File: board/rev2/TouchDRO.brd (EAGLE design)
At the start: 50.8 x 50.8 mm, 24 parts, among them U2 VREG_33, U3 VREG_5

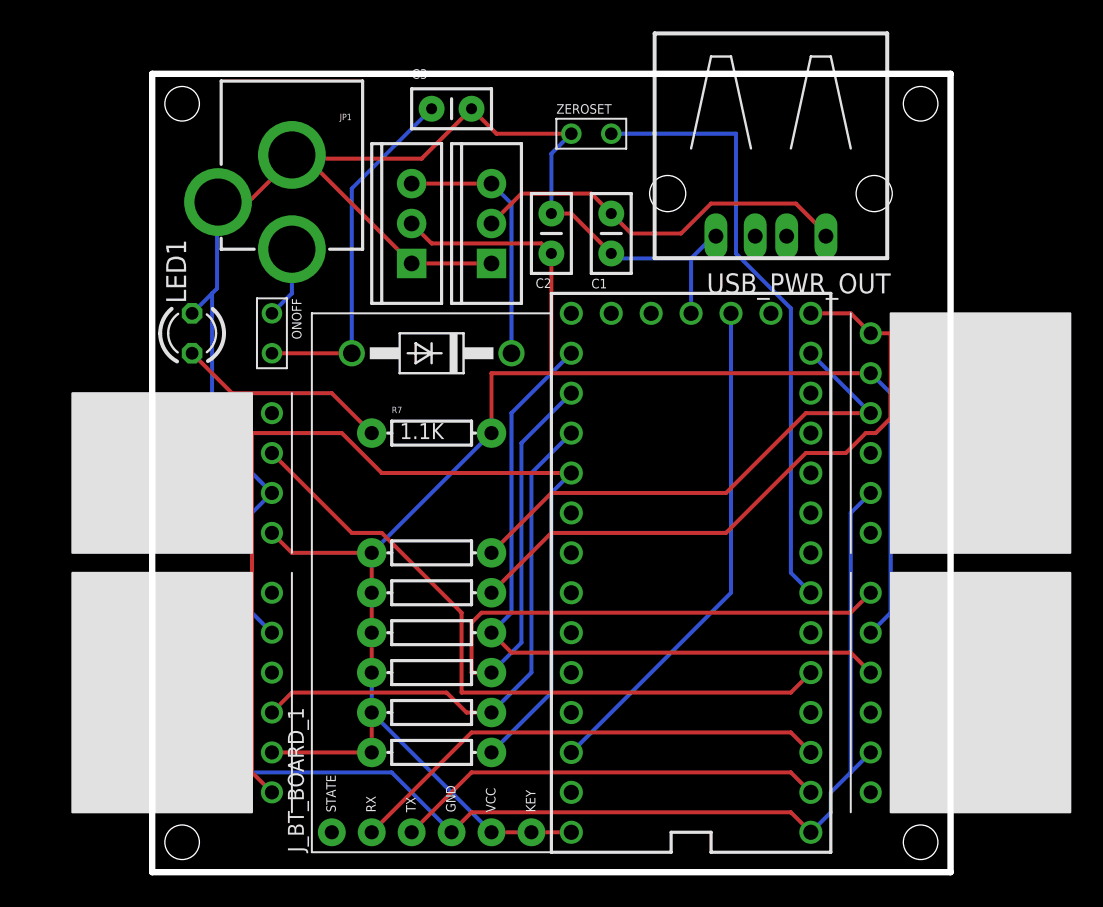
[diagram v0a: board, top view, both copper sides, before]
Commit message: adding additional caps to voltage regulator outputs
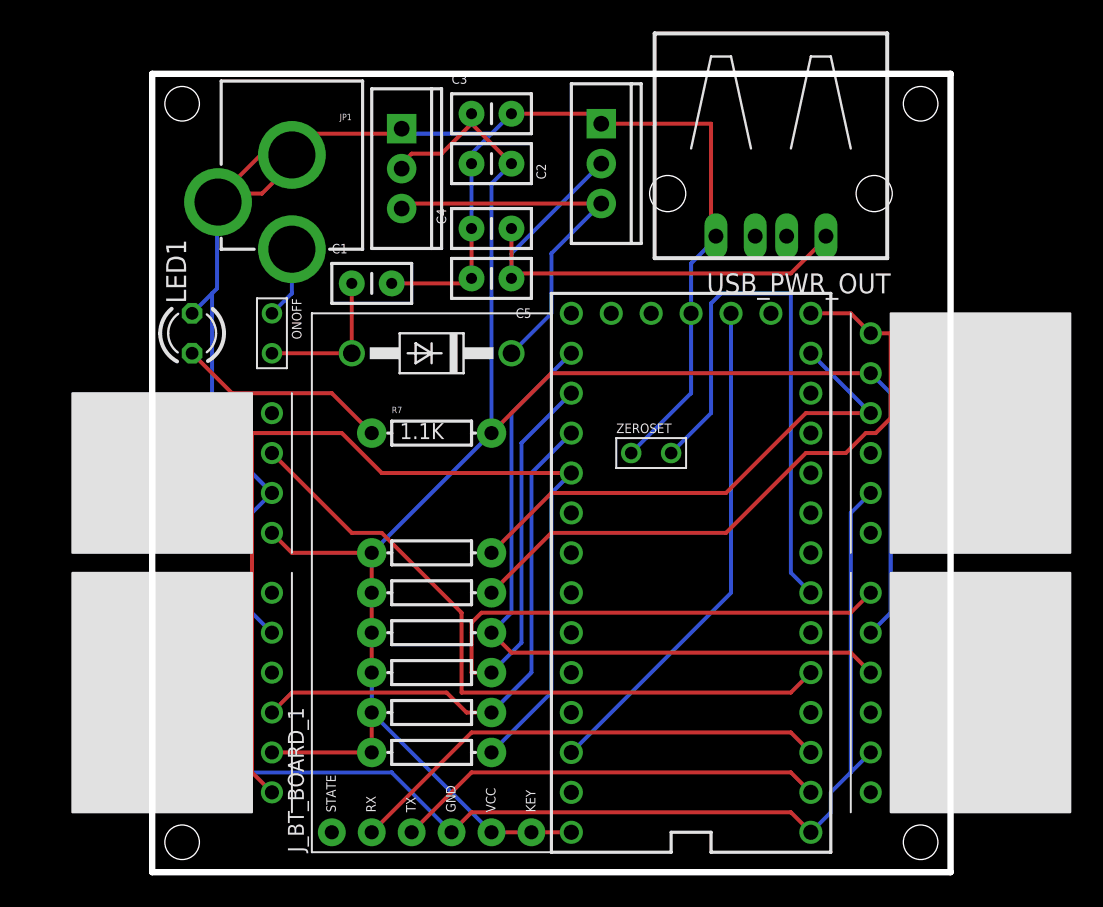
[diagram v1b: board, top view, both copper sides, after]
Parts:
- added C4: 10uF, SparkFun-Passives:CAP-PTH-SMALLEZ
- added C5: 0.1uF, SparkFun-Passives:CAP-PTH-SMALLEZ
- C1: value 10uF -> 100uF
- C3: value 100uF -> 0.1uF
- moved ZEROSET 20.7 mm to (33.0, 26.7)
- moved C1 17.1 mm to (12.7, 37.5), turned to 0 degrees
- moved U3 7.96 mm to (28.6, 45.1), turned to 270 degrees
- moved C2 6.25 mm to (22.9, 45.1), turned to 180 degrees
- moved U2 3.55 mm to (15.9, 44.8), turned to 270 degrees
- moved C3 2.56 mm to (20.3, 48.3)
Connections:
- net +3V3: now also C3.1
- net +5V: now also C4.1, C5.1; no longer C1.1
- net GND: now also C4.2, C5.2
- net ONOFF: now also C1.1; no longer C3.1
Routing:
- net GND: track 168.1 -> 184.3 mm
- net ONOFF: track 22.7 -> 9.52 mm
- net +5V: track 24.9 -> 33.9 mm
- net D1: track 16.4 -> 24.9 mm
- net +3V3: track 115.4 -> 123.5 mm
- net ZSET: track 39.1 -> 35.5 mm

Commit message: rerouting z-axis signals to new pins
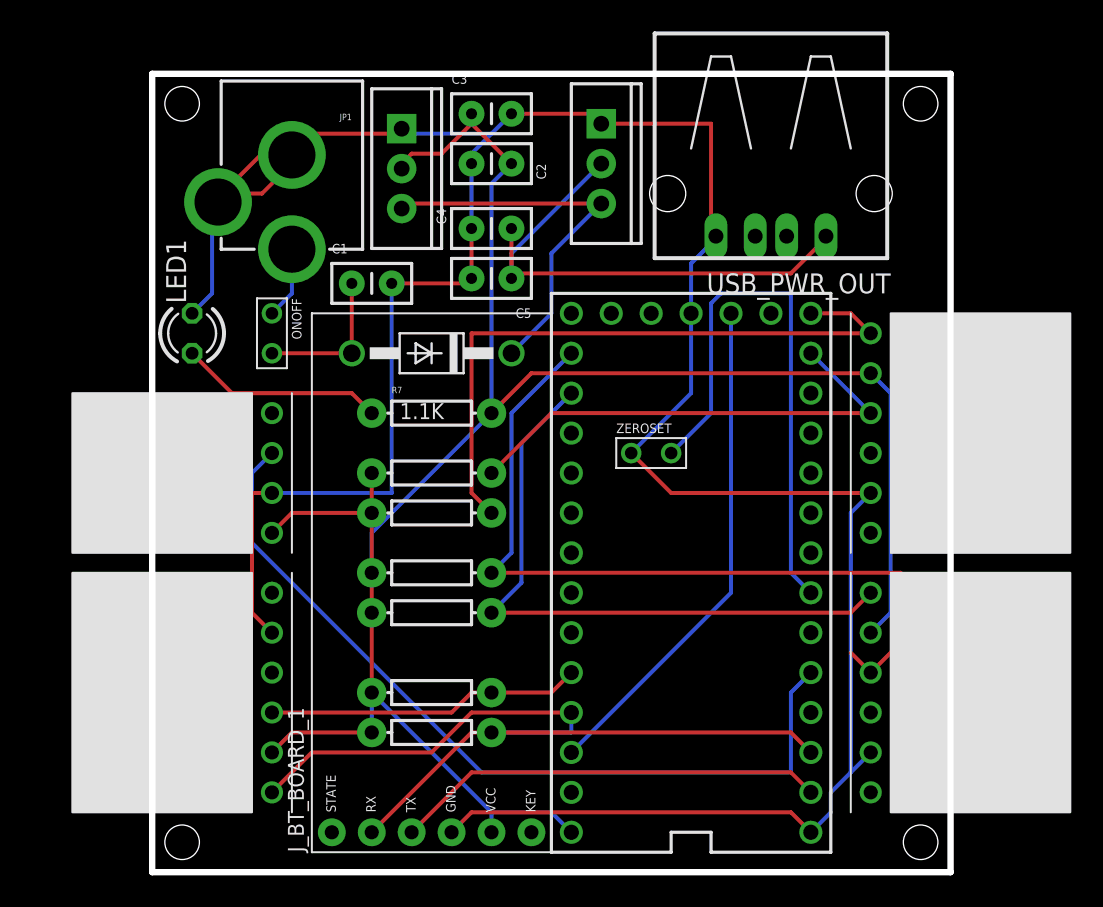
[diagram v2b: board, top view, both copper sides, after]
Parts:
- moved R1 5.08 mm to (17.8, 25.4)
- moved R2 5.08 mm to (17.8, 22.9)
- moved R4 3.81 mm to (17.8, 16.5)
- moved R3 3.81 mm to (17.8, 19.1)
- moved R6 1.27 mm to (17.8, 8.89)
- moved R5 1.27 mm to (17.8, 11.4)
- moved R7 1.27 mm to (17.8, 29.2)
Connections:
- net Z_A: now also U$1.22/A8; no longer U$1.16/A2
- net Z_B: now also U$1.23/A9; no longer U$1.17/A3
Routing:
- net Z_B: track 64.6 -> 27.5 mm
- net Z_A: track 34.9 -> 20.1 mm
- net Y_B: track 50.5 -> 40.7 mm
- net T: track 44.1 -> 53.5 mm
- net +3V3: track 123.5 -> 130.4 mm
- net Y_A: track 45.1 -> 51.0 mm
- net X_A: track 33.2 -> 31.1 mm
- net X_B: track 41.0 -> 41.7 mm
- net N$1: track 13.5 -> 13.0 mm

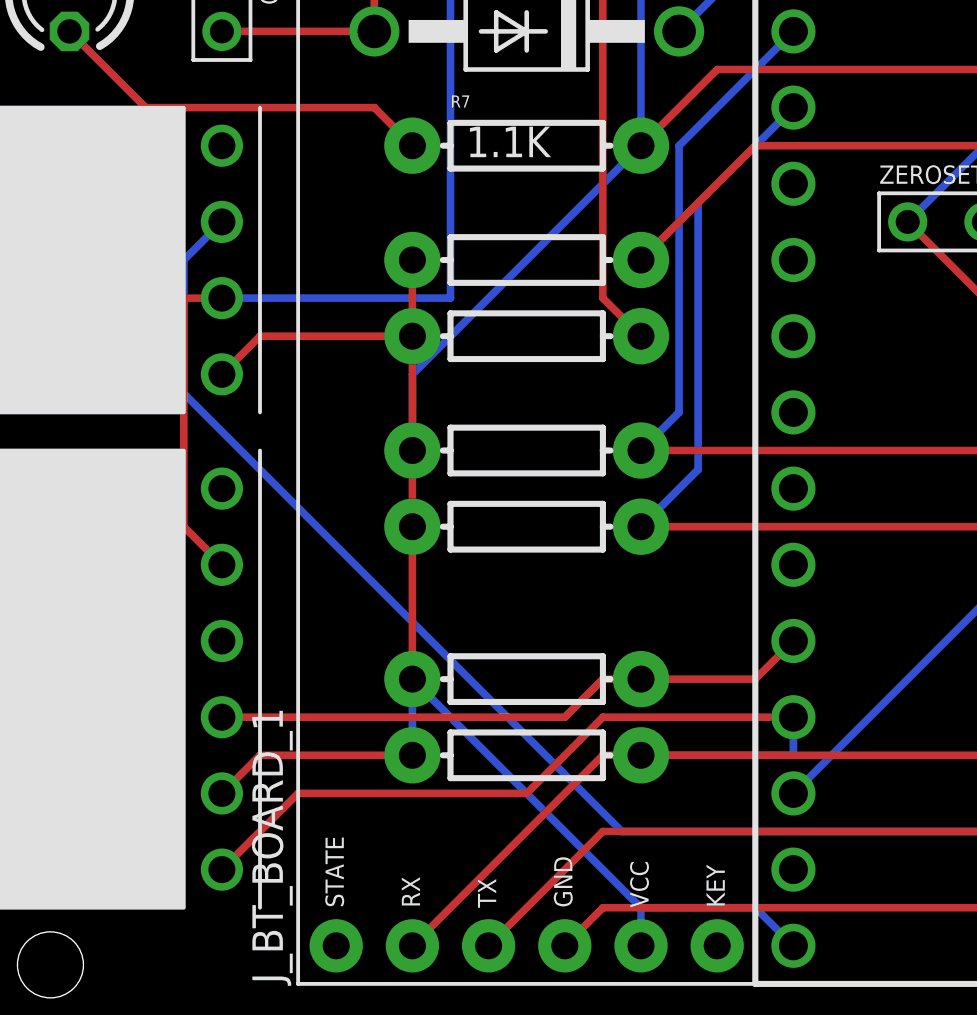
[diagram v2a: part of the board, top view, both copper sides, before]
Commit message: added dual routing of tach signal to handle 3.2 and LC versions
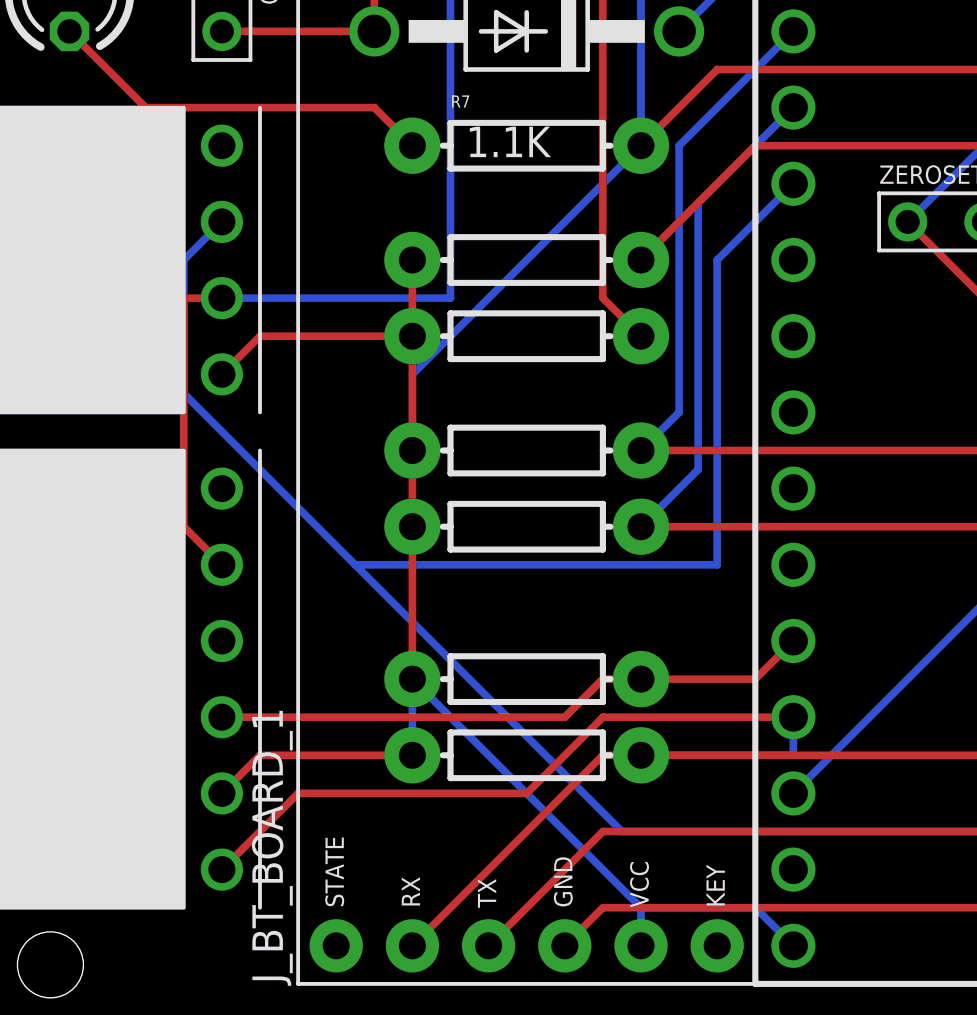
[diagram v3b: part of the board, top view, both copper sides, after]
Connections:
- net T: now also U$1.16/A2
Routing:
- net T: track 53.5 -> 79.3 mm
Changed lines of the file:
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@@
 <autorouter>
 <pass name="Default">
-<param name="RoutingGrid" value="12.5mil"/>
+<param name="RoutingGrid" value="6.25mil"/>
 <param name="AutoGrid" value="1"/>
 <param name="Efforts" value="1"/>
 <param name="TopRouterVariant" value="1"/>
 <param name="tpViaShape" value="round"/>
-<param name="PrefDir.1" value="a"/>
+<param name="PrefDir.1" value="*"/>
 <param name="PrefDir.2" value="0"/>
 <param name="PrefDir.3" value="0"/>
@@
 <param name="PrefDir.14" value="0"/>
 <param name="PrefDir.15" value="0"/>
-<param name="PrefDir.16" value="a"/>
+<param name="PrefDir.16" value="*"/>
 <param name="cfVia" value="8"/>
 <param name="cfNonPref" value="5"/>
@@
 <wire x1="6.35" y1="25.4" x2="7.62" y2="26.67" width="0.254" layer="16"/>
 <wire x1="6.35" y1="20.955" x2="6.35" y2="25.4" width="0.254" layer="16"/>
-<wire x1="20.955" y1="6.35" x2="6.35" y2="20.955" width="0.254" layer="16"/>
+<wire x1="20.955" y1="6.35" x2="12.065" y2="15.24" width="0.254" layer="16"/>
+<wire x1="12.065" y1="15.24" x2="6.35" y2="20.955" width="0.254" layer="16"/>
 <wire x1="40.64" y1="6.35" x2="20.955" y2="6.35" width="0.254" layer="16"/>
 <wire x1="40.64" y1="11.43" x2="40.64" y2="6.35" width="0.254" layer="16"/>
 <wire x1="41.91" y1="12.7" x2="40.64" y2="11.43" width="0.254" layer="16"/>
+<contactref element="U$1" pad="16/A2"/>
+<wire x1="24.13" y1="25.4" x2="26.67" y2="27.94" width="0.254" layer="16"/>
+<wire x1="24.13" y1="15.24" x2="24.13" y2="25.4" width="0.254" layer="16"/>
+<wire x1="12.065" y1="15.24" x2="24.13" y2="15.24" width="0.254" layer="16"/>
 </signal>
 <signal name="N$6">
